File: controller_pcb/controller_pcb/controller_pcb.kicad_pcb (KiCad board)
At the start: 2 copper layers, 34 parts, among them J1 USB_B_Micro, Y1 8MHz

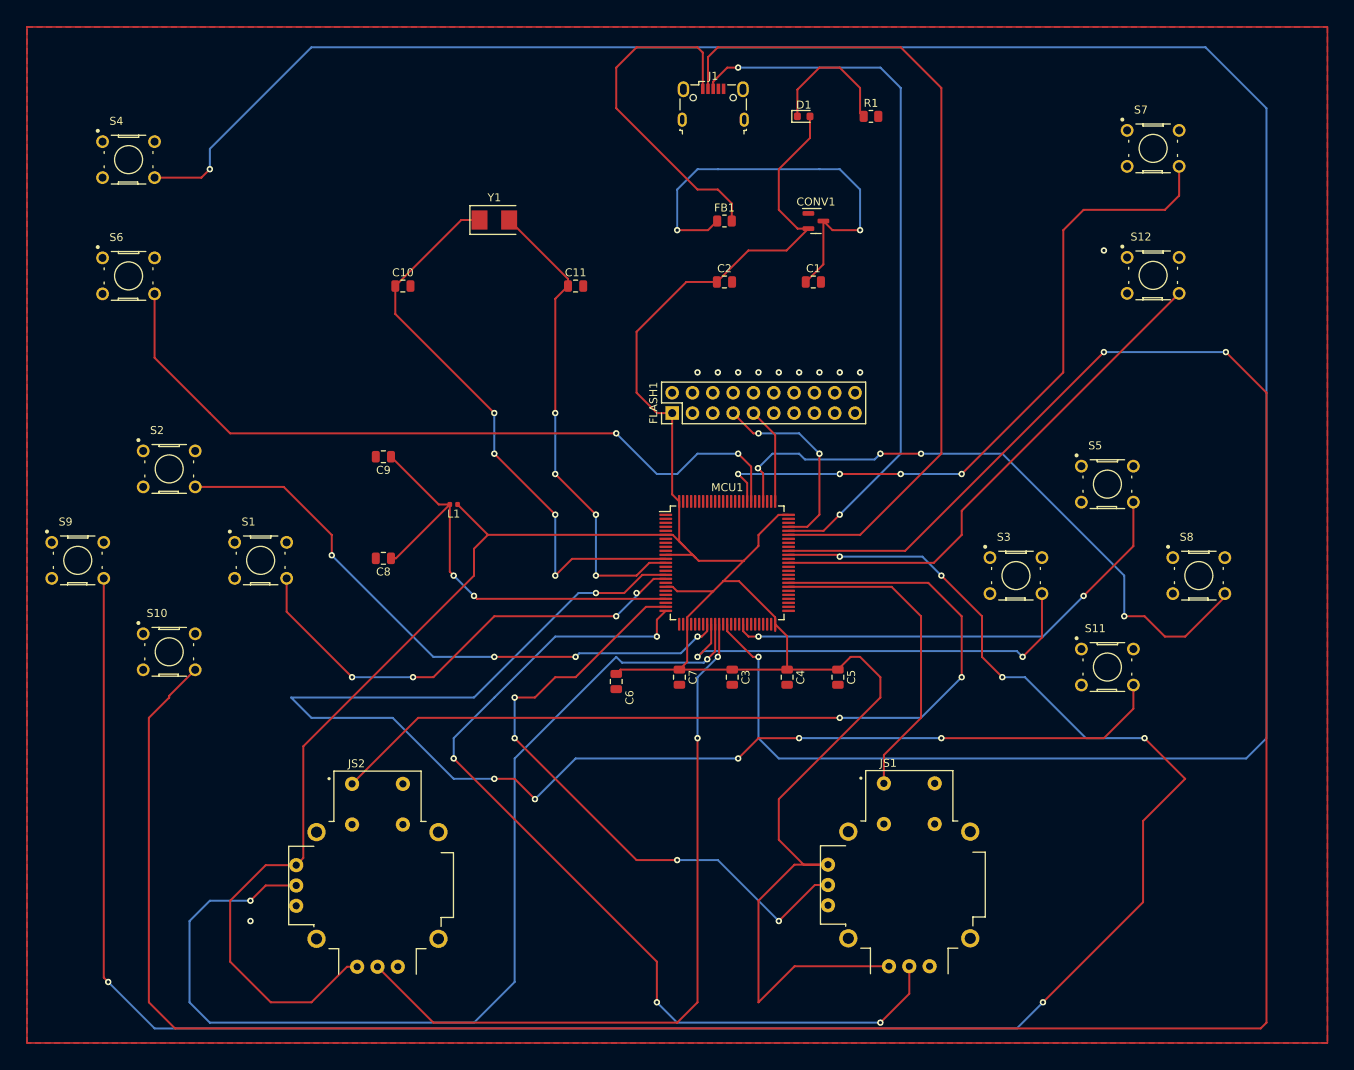
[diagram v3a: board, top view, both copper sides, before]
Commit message: fixed drc warnings and errors in pcb
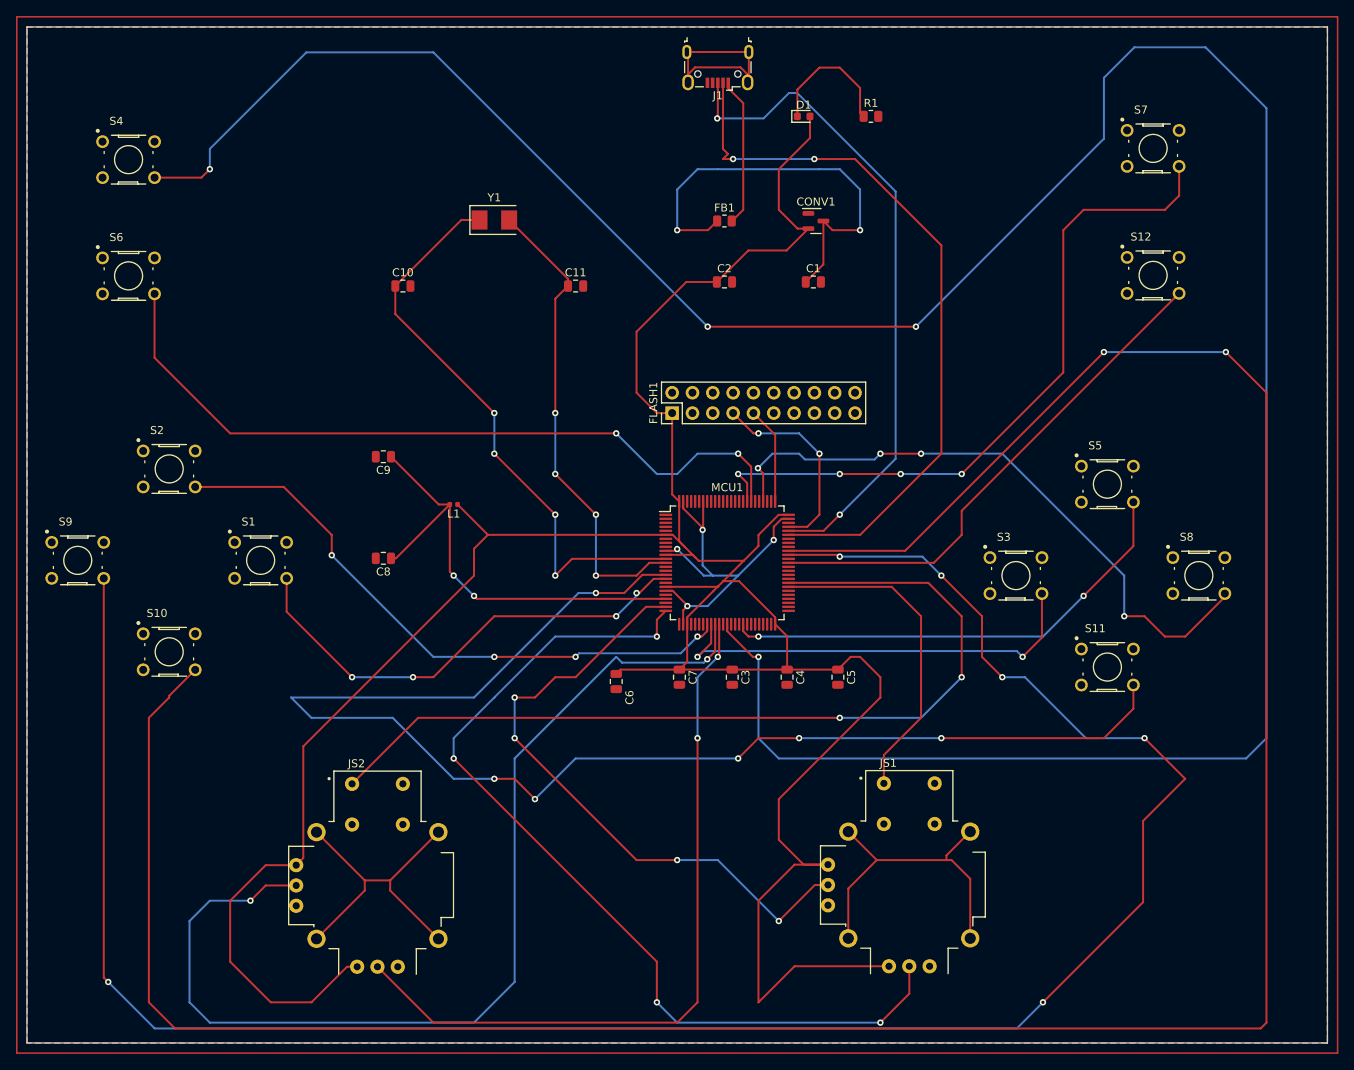
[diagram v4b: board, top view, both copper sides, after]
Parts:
- moved J1 4.59 mm to (157.5, 43.2), turned to 180 degrees
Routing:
- net GND: track 0.00 -> 49.1 mm, vias 0 -> 4
- net Net-(JS1-PadS1): track 0.00 -> 41.2 mm
- net Net-(JS2-PadS1): track 0.00 -> 39.8 mm
- net PE7: track 311.0 -> 343.9 mm, vias 2 -> 4
- net unconnected-(J1-Pad6): track 0.00 -> 25.7 mm
- net +5V: track 43.3 -> 18.7 mm
- net USB_DM: track 104.8 -> 91.2 mm, vias 0 -> 2
- net USB_DP: track 89.9 -> 83.7 mm
- net (no net): vias 11 -> 0
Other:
- board outline added: 162.6 x 127 mm

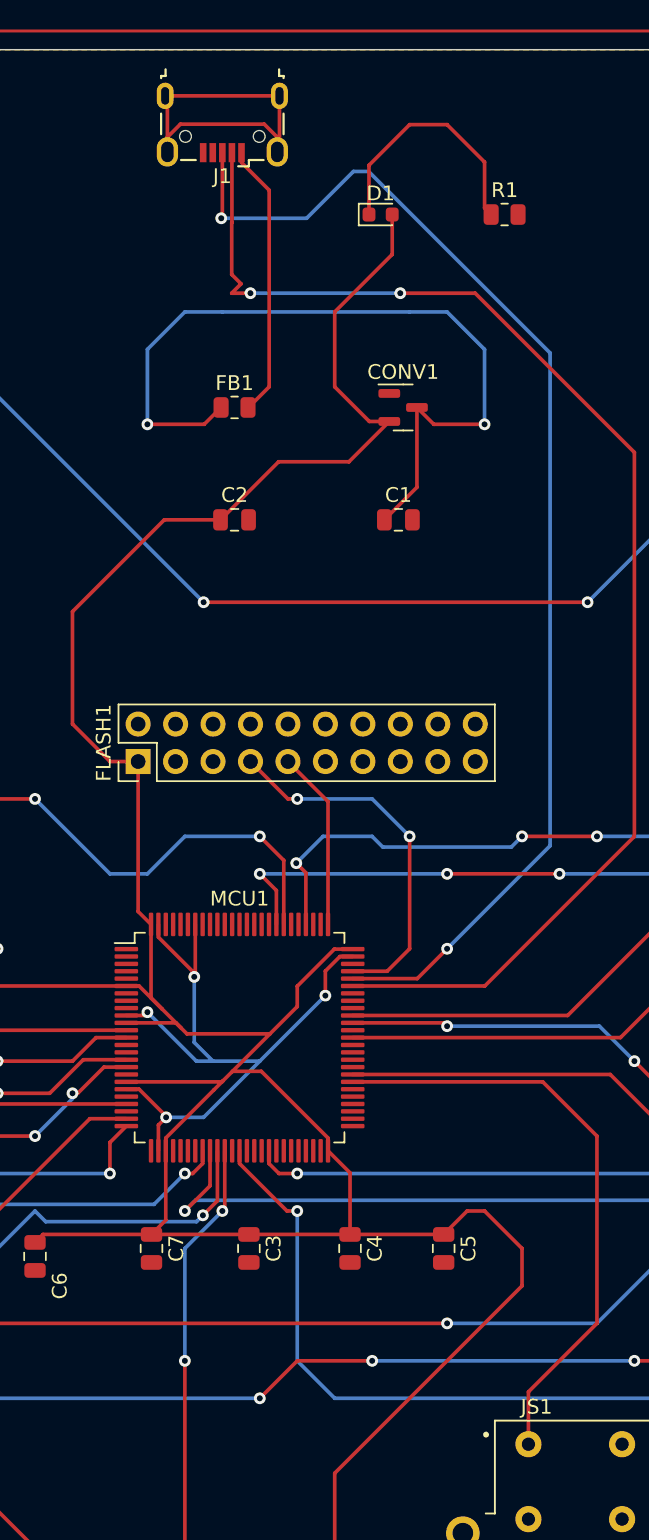
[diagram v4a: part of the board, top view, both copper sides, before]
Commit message: moved silkscreen
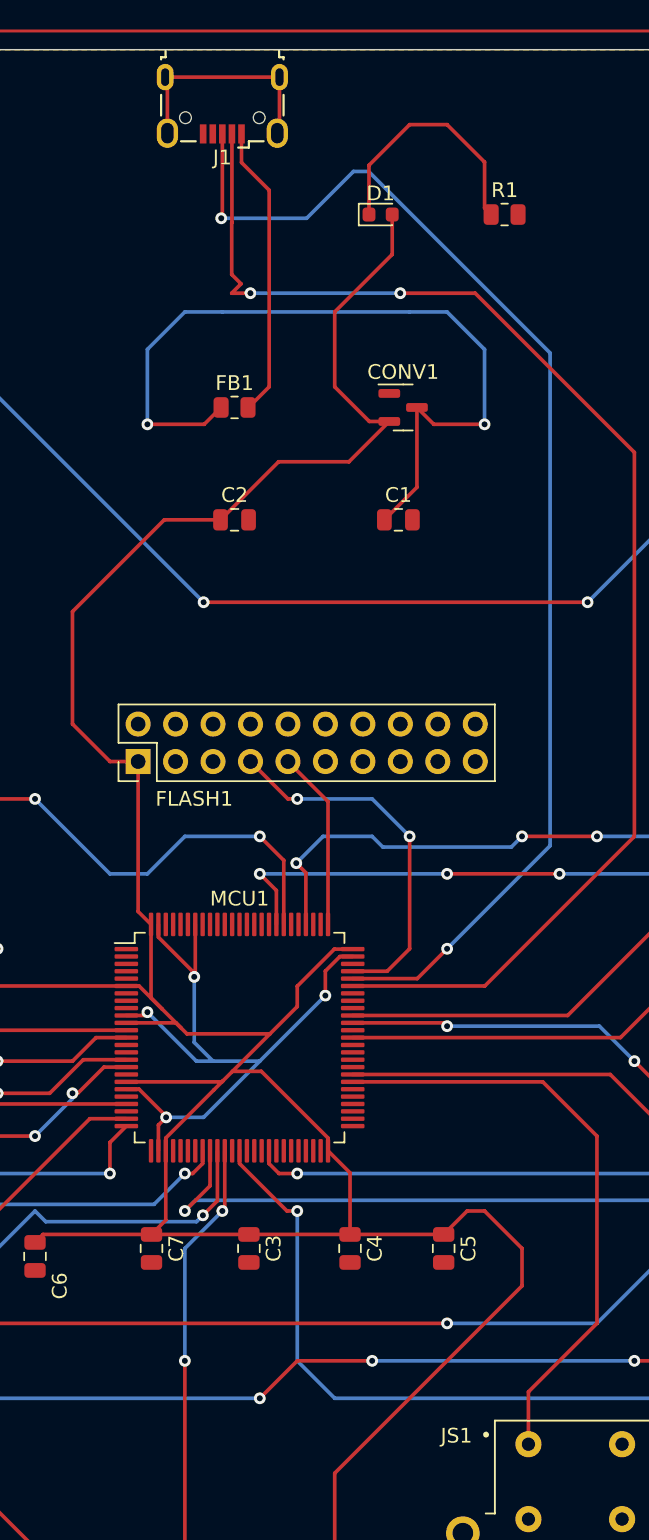
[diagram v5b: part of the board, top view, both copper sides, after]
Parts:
- moved J1 1.27 mm to (157.5, 41.9)
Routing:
- net unconnected-(J1-Pad6): track 25.7 -> 15.5 mm
- net USB_DP: track 83.7 -> 85.0 mm
- net USB_DM: track 91.2 -> 92.4 mm
- net +5V: track 18.7 -> 19.9 mm
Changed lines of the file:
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@@
     (property "Sheetname" "")
     (attr through_hole)
-    (fp_text reference "FLASH1" (at 1.27 -2.33 90) (layer "F.SilkS")
+    (fp_text reference "FLASH1" (at -2.535 3.805 180) (layer "F.SilkS")
       (effects (font (size 1 1) (thickness 0.15)))
     )
@@
       (effects (font (size 1.000008 1.000008) (thickness 0.15)))
     )
-    (fp_text value "B3F-1000" (at 2.341095 4.352635) (layer "F.Fab")
+    (fp_text value "B3F-1000" (at -3.61 4.507154) (layer "F.Fab")
       (effects (font (size 1.001756 1.001756) (thickness 0.15)))
     )
@@
   )
   (footprint "Connector_USB:USB_Micro-B_Wuerth_629105150521" (layer "F.Cu")
-    (at 157.48 43.18 180)
+    (at 157.48 41.91 180)
     (descr "USB Micro-B receptacle, http://www.mouser.com/ds/2/445/629105150521-469306.pdf")
     (tags "usb micro receptacle")
@@
       (effects (font (size 1 1) (thickness 0.15)))
     )
-    (fp_text value "USB_B_Micro" (at 0 5.6) (layer "F.Fab")
+    (fp_text value "USB_B_Micro" (at 10.16 -0.635) (layer "F.Fab")
       (effects (font (size 1 1) (thickness 0.15)))
     )
@@
       (effects (font (size 1 1) (thickness 0.15)))
     )
-    (fp_text value "XC6206PxxxMR" (at 0 2.4) (layer "F.Fab")
+    (fp_text value "XC6206PxxxMR" (at 6.792 2.4 -90) (layer "F.Fab")
       (effects (font (size 1 1) (thickness 0.15)))
     )
@@
       (effects (font (size 1.000008 1.000008) (thickness 0.15)))
     )
-    (fp_text value "B3F-1000" (at 2.341095 4.352635) (layer "F.Fab")
+    (fp_text value "B3F-1000" (at -1.705 4.507154) (layer "F.Fab")
       (effects (font (size 1.001756 1.001756) (thickness 0.15)))
     )
@@
     (property "Sheetname" "")
     (attr through_hole)
-    (fp_text reference "JS1" (at -2.625 -15.235) (layer "F.SilkS")
-      (effects (font (size 1 1) (thickness 0.15)))
-    )
-    (fp_text value "COM-09032" (at 3.09 14.265) (layer "F.Fab")
+    (fp_text reference "JS1" (at -8.055 -13.272846) (layer "F.SilkS")
+      (effects (font (size 1 1) (thickness 0.15)))
+    )
+    (fp_text value "COM-09032" (at 5.915 14.265) (layer "F.Fab")
       (effects (font (size 1 1) (thickness 0.15)))
     )
@@
   (segment (start 172.72 43.18) (end 170.18 43.18) (width 0.25) (layer "F.Cu") (net 5))
   (segment (start 167.424 45.936) (end 167.424 49.276) (width 0.25) (layer "F.Cu") (net 5))
-  (segment (start 158.78 45.75) (end 160.655 47.625) (width 0.25) (layer "F.Cu") (net 6))
-  (segment (start 160.655 47.625) (end 160.655 60.96) (width 0.25) (layer "F.Cu") (net 6))
-  (segment (start 158.78 45.08) (end 158.78 45.75) (width 0.25) (layer "F.Cu") (net 6))
-  (segment (start 159.258 62.357) (end 159.2205 62.357) (width 0.25) (layer "F.Cu") (net 6))
-  (segment (start 160.655 60.96) (end 159.258 62.357) (width 0.25) (layer "F.Cu") (net 6))
+  (segment (start 158.78 45.75) (end 158.78 43.81) (width 0.25) (layer "F.Cu") (net 6))
+  (segment (start 160.655 47.625) (end 158.78 45.75) (width 0.25) (layer "F.Cu") (net 6))
+  (segment (start 159.2205 62.357) (end 159.258 62.357) (width 0.25) (layer "F.Cu") (net 6))
+  (segment (start 160.655 60.96) (end 160.655 47.625) (width 0.25) (layer "F.Cu") (net 6))
+  (segment (start 159.258 62.357) (end 160.655 60.96) (width 0.25) (layer "F.Cu") (net 6))
+  (segment (start 174.625 54.61) (end 169.545 54.61) (width 0.25) (layer "F.Cu") (net 7))
+  (segment (start 158.115 49.845805) (end 158.13 49.830805) (width 0.25) (layer "F.Cu") (net 7))
+  (segment (start 158.75 53.975) (end 158.115 53.34) (width 0.25) (layer "F.Cu") (net 7))
+  (segment (start 159.385 54.61) (end 158.115 54.61) (width 0.25) (layer "F.Cu") (net 7))
   (segment (start 158.115 53.34) (end 158.115 49.845805) (width 0.25) (layer "F.Cu") (net 7))
-  (segment (start 174.625 54.61) (end 169.545 54.61) (width 0.25) (layer "F.Cu") (net 7))
-  (segment (start 159.385 54.61) (end 158.115 54.61) (width 0.25) (layer "F.Cu") (net 7))
-  (segment (start 158.115 54.61) (end 158.75 53.975) (width 0.25) (layer "F.Cu") (net 7))
-  (segment (start 158.115 49.845805) (end 158.13 49.830805) (width 0.25) (layer "F.Cu") (net 7))
   (segment (start 175.276 101.584) (end 166.321 101.584) (width 0.25) (layer "F.Cu") (net 7))
+  (segment (start 158.13 49.830805) (end 158.13 43.81) (width 0.25) (layer "F.Cu") (net 7))
   (segment (start 185.42 91.44) (end 175.276 101.584) (width 0.25) (layer "F.Cu") (net 7))
   (segment (start 185.42 65.405) (end 174.625 54.61) (width 0.25) (layer "F.Cu") (net 7))
   (segment (start 185.42 91.44) (end 185.42 65.405) (width 0.25) (layer "F.Cu") (net 7))
-  (segment (start 158.13 49.830805) (end 158.13 45.08) (width 0.25) (layer "F.Cu") (net 7))
-  (segment (start 158.75 53.975) (end 158.115 53.34) (width 0.25) (layer "F.Cu") (net 7))
+  (segment (start 158.115 54.61) (end 158.75 53.975) (width 0.25) (layer "F.Cu") (net 7))
   (via (at 169.545 54.61) (size 0.8) (drill 0.4) (layers "F.Cu" "B.Cu") (net 7))
   (via (at 159.385 54.61) (size 0.8) (drill 0.4) (layers "F.Cu" "B.Cu") (net 7))
@@
   (segment (start 172.72 99.06) (end 170.696 101.084) (width 0.25) (layer "F.Cu") (net 8))
   (segment (start 170.696 101.084) (end 166.321 101.084) (width 0.25) (layer "F.Cu") (net 8))
-  (segment (start 157.48 49.4555) (end 157.48 45.08) (width 0.25) (layer "F.Cu") (net 8))
+  (segment (start 157.48 49.4555) (end 157.48 43.81) (width 0.25) (layer "F.Cu") (net 8))
   (segment (start 157.4055 49.53) (end 157.48 49.4555) (width 0.25) (layer "F.Cu") (net 8))
   (via (at 172.72 99.06) (size 0.8) (drill 0.4) (layers "F.Cu" "B.Cu") (net 8))
@@
   (segment (start 179.705 92.075) (end 179.705 58.664695) (width 0.25) (layer "B.Cu") (net 8))
   (segment (start 179.705 58.664695) (end 167.395305 46.355) (width 0.25) (layer "B.Cu") (net 8))
-  (segment (start 161.205 44.031484) (end 161.205 45.03) (width 0.25) (layer "F.Cu") (net 10))
-  (segment (start 161.355 41.23) (end 161.355 44.88) (width 0.25) (layer "F.Cu") (net 10))
-  (segment (start 161.355 44.88) (end 161.205 45.03) (width 0.25) (layer "F.Cu") (net 10))
-  (segment (start 153.755 45.03) (end 153.755 44.031484) (width 0.25) (layer "F.Cu") (net 10))
-  (segment (start 153.605 41.23) (end 161.355 41.23) (width 0.25) (layer "F.Cu") (net 10))
-  (segment (start 153.755 44.031484) (end 154.636285 43.150199) (width 0.25) (layer "F.Cu") (net 10))
-  (segment (start 160.323715 43.150199) (end 161.205 44.031484) (width 0.25) (layer "F.Cu") (net 10))
-  (segment (start 154.636285 43.150199) (end 160.323715 43.150199) (width 0.25) (layer "F.Cu") (net 10))
-  (segment (start 153.755 45.03) (end 153.755 41.38) (width 0.25) (layer "F.Cu") (net 10))
-  (segment (start 153.755 41.38) (end 153.605 41.23) (width 0.25) (layer "F.Cu") (net 10))
+  (segment (start 153.755 40.11) (end 153.605 39.96) (width 0.25) (layer "F.Cu") (net 10))
+  (segment (start 161.355 43.61) (end 161.205 43.76) (width 0.25) (layer "F.Cu") (net 10))
+  (segment (start 161.355 39.96) (end 161.355 43.61) (width 0.25) (layer "F.Cu") (net 10))
+  (segment (start 153.755 43.76) (end 153.755 40.11) (width 0.25) (layer "F.Cu") (net 10))
+  (segment (start 153.605 39.96) (end 161.355 39.96) (width 0.25) (layer "F.Cu") (net 10))
   (segment (start 117.16 73.98) (end 129.54 86.36) (width 0.25) (layer "F.Cu") (net 11))
   (segment (start 137.16 106.68) (end 139.256 104.584) (width 0.25) (layer "F.Cu") (net 11))

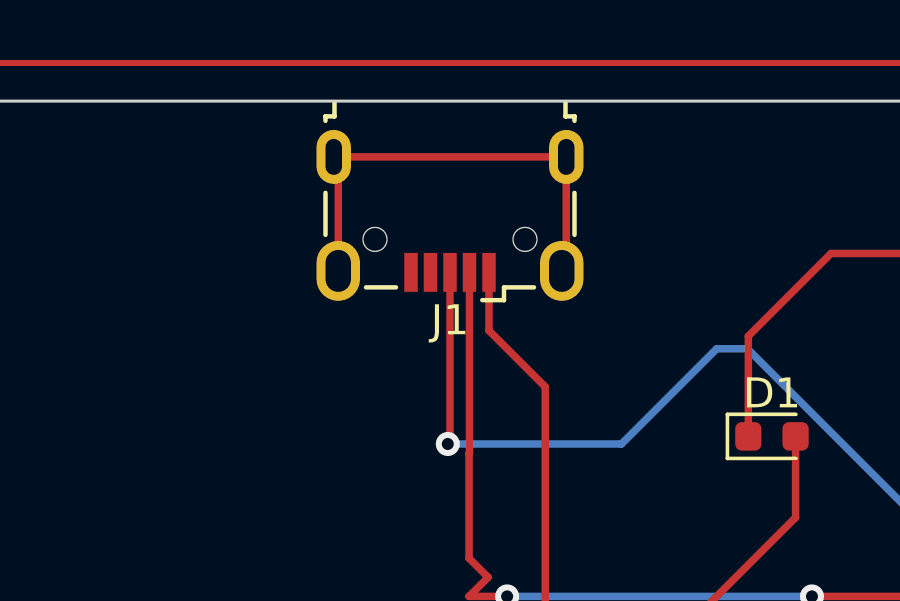
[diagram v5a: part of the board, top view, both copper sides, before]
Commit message: Made a small GND connection to USB Micro
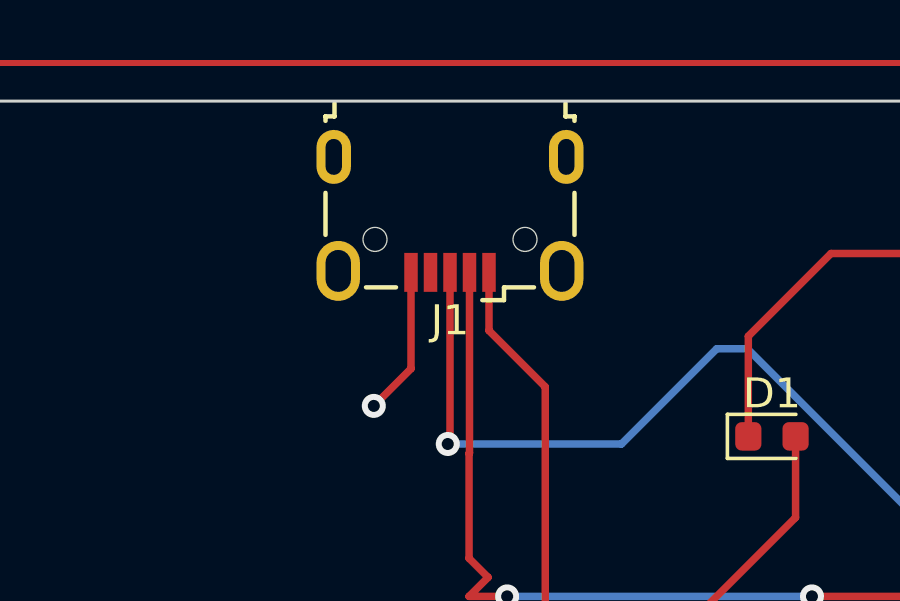
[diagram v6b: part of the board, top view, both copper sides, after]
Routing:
- net unconnected-(J1-Pad6): track 15.5 -> 0.42 mm
- net GND: track 49.1 -> 54.1 mm, vias 4 -> 5
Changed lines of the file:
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@@
   (segment (start 164.465 100.574315) (end 164.465 102.235) (width 0.25) (layer "F.Cu") (net 2))
   (segment (start 152.321 103.584) (end 152.4 103.505) (width 0.25) (layer "F.Cu") (net 2))
+  (segment (start 156.18 47.02) (end 154.94 48.26) (width 0.25) (layer "F.Cu") (net 2))
+  (segment (start 156.18 43.81) (end 156.18 47.02) (width 0.25) (layer "F.Cu") (net 2))
   (segment (start 155.646 100.894) (end 155.646 97.409) (width 0.25) (layer "F.Cu") (net 2))
   (segment (start 153.146 98.274685) (end 155.575 100.703685) (width 0.25) (layer "F.Cu") (net 2))
@@
   (via (at 155.575 100.965) (size 0.8) (drill 0.4) (layers "F.Cu" "B.Cu") (net 2))
   (via (at 164.465 102.235) (size 0.8) (drill 0.4) (layers "F.Cu" "B.Cu") (net 2))
+  (via (at 154.94 48.26) (size 0.8) (drill 0.4) (layers "F.Cu" "B.Cu") (net 2))
   (segment (start 160.02 106.68) (end 156.21 110.49) (width 0.25) (layer "B.Cu") (net 2))
   (segment (start 155.575 105.41) (end 156.845 106.68) (width 0.25) (layer "B.Cu") (net 2))
@@
   (segment (start 153.755 40.11) (end 153.605 39.96) (width 0.25) (layer "F.Cu") (net 10))
   (segment (start 161.355 43.61) (end 161.205 43.76) (width 0.25) (layer "F.Cu") (net 10))
-  (segment (start 161.355 39.96) (end 161.355 43.61) (width 0.25) (layer "F.Cu") (net 10))
-  (segment (start 153.755 43.76) (end 153.755 40.11) (width 0.25) (layer "F.Cu") (net 10))
-  (segment (start 153.605 39.96) (end 161.355 39.96) (width 0.25) (layer "F.Cu") (net 10))
   (segment (start 117.16 73.98) (end 129.54 86.36) (width 0.25) (layer "F.Cu") (net 11))
   (segment (start 137.16 106.68) (end 139.256 104.584) (width 0.25) (layer "F.Cu") (net 11))
